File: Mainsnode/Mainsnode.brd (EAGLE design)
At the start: 60.9 x 31.7 mm, 30 parts, among them IC1 LTC-1966MSOP-8, IC2 LTC-1966MSOP-8, IC3 LD117AS33TR

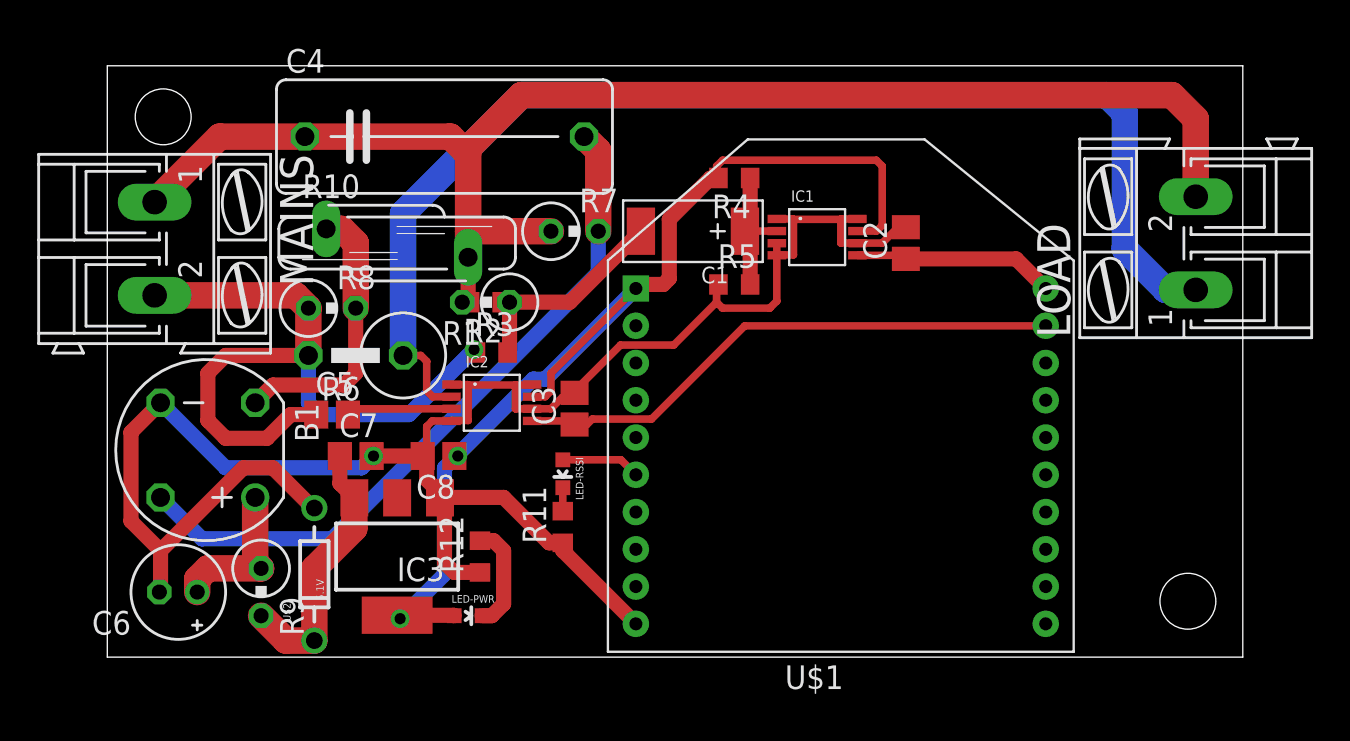
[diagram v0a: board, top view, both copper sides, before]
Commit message: Add ACS712, 5V supply, conditioner 3.3V
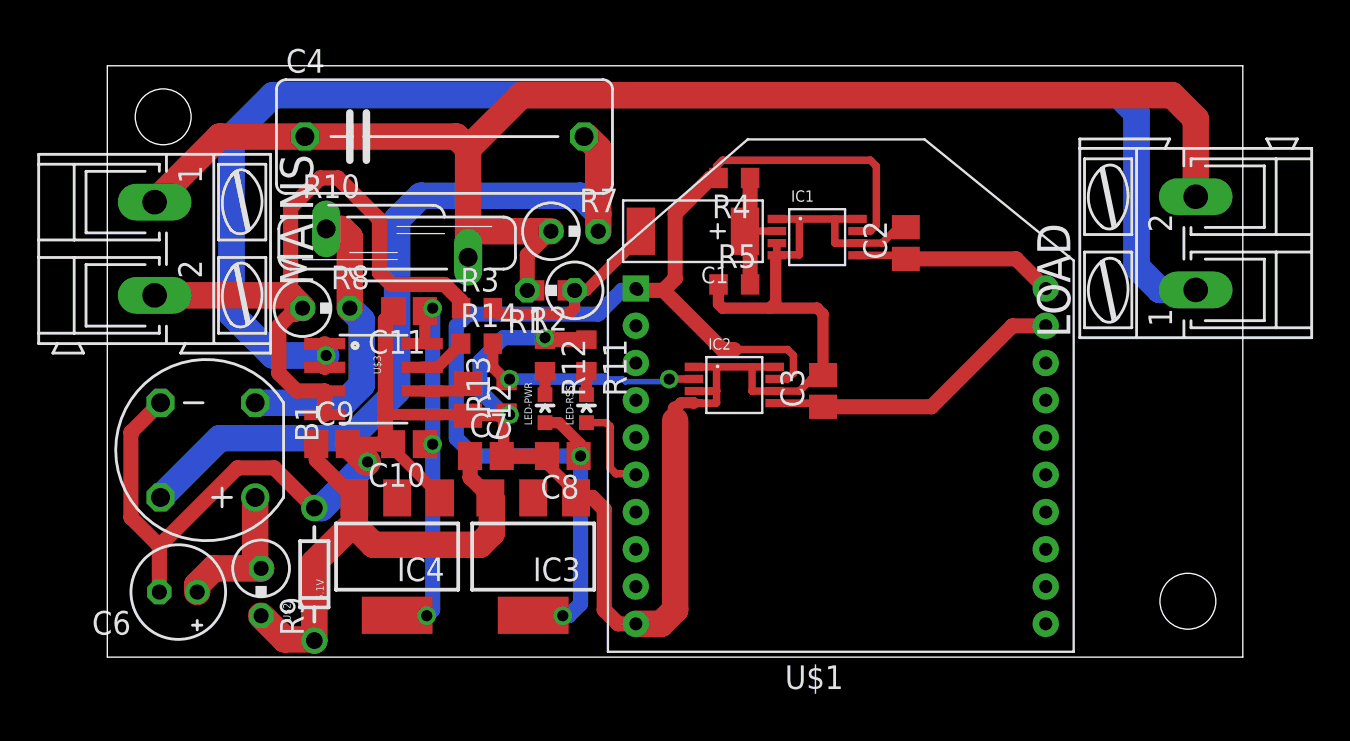
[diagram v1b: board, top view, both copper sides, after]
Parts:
- removed C5: C0.1uF, resistor:C0805
- removed R6: R0.1R, resistor:P0613V
- added C10, C9: C1uF, resistor:C0805
- added C11: C0.1uF, resistor:C0805
- added C12: C1nF, resistor:C0805
- added IC4: LD117AS50TR, v-reg:SOT223
- added R13: R47K, resistor:R0603
- added R14: R27K, resistor:R0603
- added U$3: ACS712, SparkFun-AnalogIC:SO08
- moved C3 13.4 mm to (38.4, 14.3)
- moved IC2 13.1 mm to (33.7, 14.6)
- moved LED-PWR 11.9 mm to (23.5, 13.3), turned to 0 degrees
- moved R12 11.3 mm to (23.5, 16.2), turned to 270 degrees
- moved R11 9.29 mm to (25.7, 16.2), turned to 270 degrees
- moved IC3 7.30 mm to (22.9, 5.40)
- moved C7 6.98 mm to (20.3, 10.8)
- moved C8 6.67 mm to (24.4, 10.8)
- moved LED-RSSI 3.72 mm to (25.7, 13.3), turned to 0 degrees
- moved R1 3.55 mm to (23.8, 19.7)
- moved R2 3.55 mm to (23.8, 19.7)
- moved R3 2.51 mm to (19.8, 18.7)
- moved R8 0.32 mm to (11.7, 18.7)
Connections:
- removed net N$2: C5.2, IC2.P$3
- new net CUR-SNSR: IC2.P$2, R13.2, R14.2
- new net N$7: C12.1, U$3.6
- new net N$9: R14.1, U$3.7
- new net V-SUPPLY: C7.1, C9.1, IC3.3, IC4.3, R9.2, U$2.P$1
- net 5V: now also C10.1, C11.1, IC4.4, U$3.8; no longer C7.1, IC3.3, R9.2, U$2.P$1
- net GND: now also C10.2, C11.2, C12.2, C9.2, IC2.P$3, IC4.1, R13.1, U$3.5
- net LOAD-NEUTRAL: now also U$3.1, U$3.2; no longer IC2.P$2, R6.1
- net MAINS-NEUTRAL: now also U$3.3, U$3.4; no longer C5.1, R6.2
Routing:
- net V-SUPPLY: track 0.00 -> 29.9 mm
- net GND: track 105.0 -> 130.4 mm, vias 1 -> 3
- net LOAD-NEUTRAL: track 65.9 -> 79.3 mm, vias 0 -> 1
- net AN-IN-CUR: track 29.8 -> 16.4 mm
- net CUR-SNSR: track 0.00 -> 12.5 mm, vias 0 -> 2
- net 3.3V: track 58.6 -> 70.9 mm, vias 2 -> 3
- net 5V: track 14.5 -> 20.9 mm, vias 0 -> 3
- net N$2: track 5.69 -> 0.00 mm
- net N$8: track 5.77 -> 1.26 mm
- net N$5: track 38.0 -> 42.4 mm
- net MAINS-NEUTRAL: track 39.5 -> 35.9 mm, vias 1 -> 0
- net N$7: track 0.00 -> 2.62 mm
- net N$9: track 0.00 -> 2.62 mm
- net LIVE: track 76.7 -> 77.9 mm
- net RSSI: track 4.26 -> 5.11 mm
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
